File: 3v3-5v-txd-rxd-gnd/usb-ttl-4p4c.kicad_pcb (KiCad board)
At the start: 4 copper layers, 41.3 x 14 mm, 3 parts, among them J1 4P4C, P1 CONN_5X1

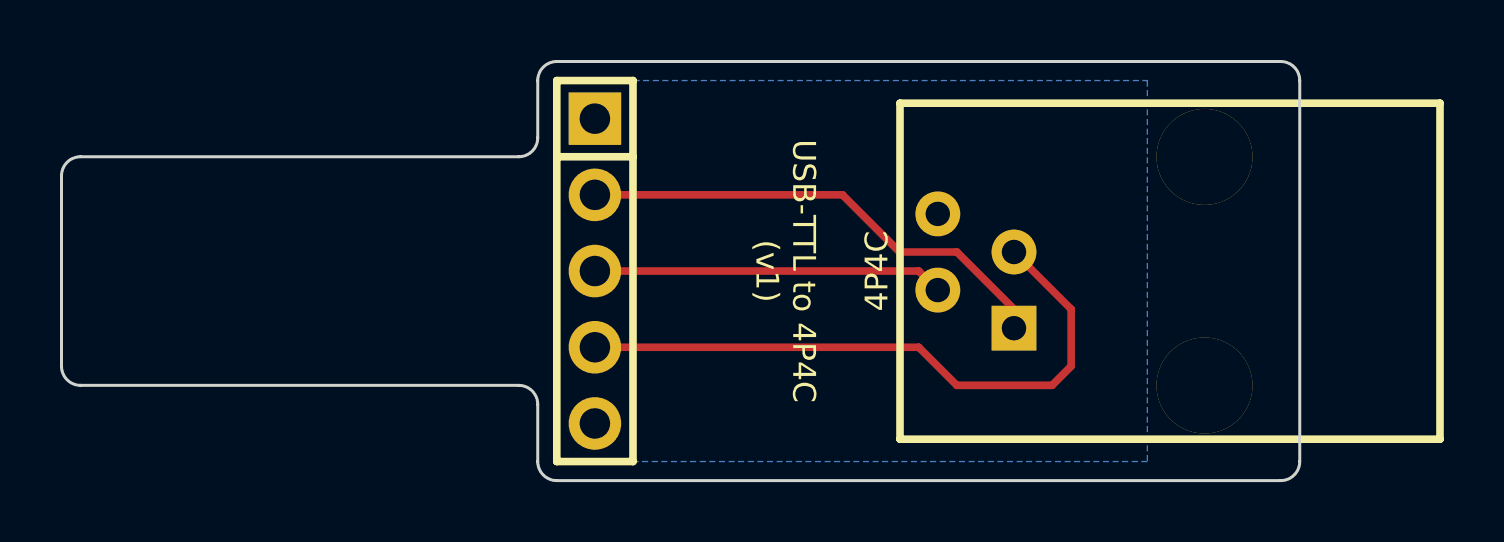
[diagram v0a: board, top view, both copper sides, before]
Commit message: adding a diode
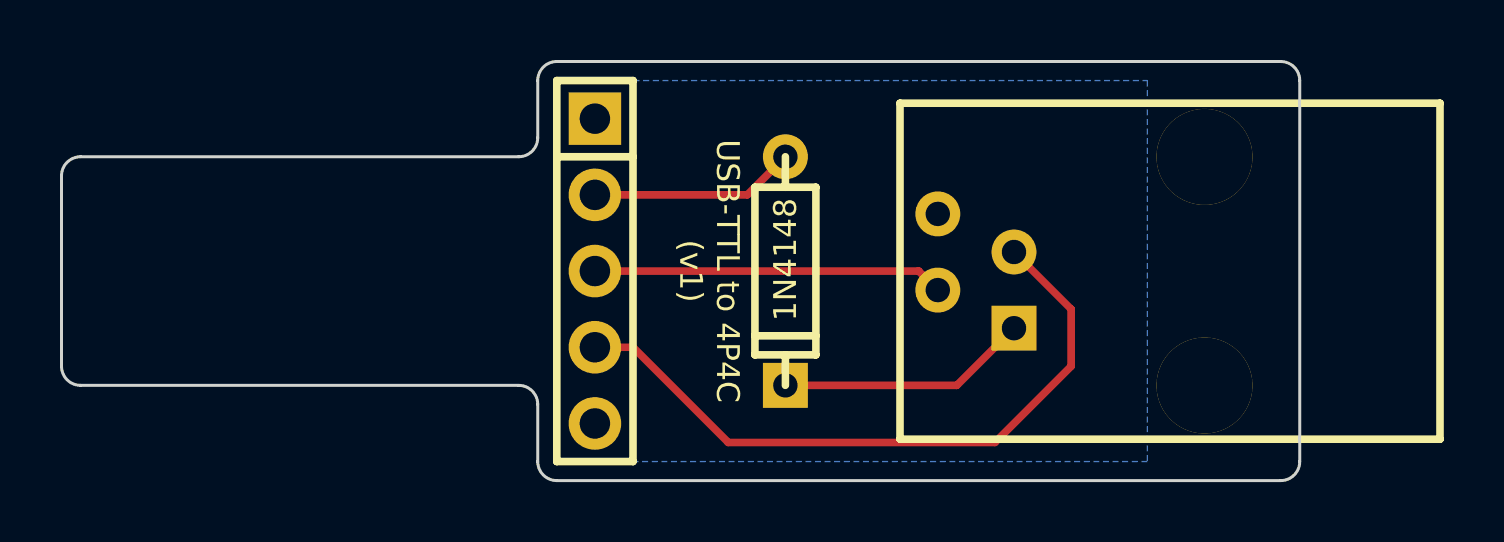
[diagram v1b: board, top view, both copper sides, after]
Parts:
- added D1: 1N4148, DIODE_SS_059A_03_PL, F.Cu at (180.3, 111.1)
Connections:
- J1 pad 1: 5V -> N-000006
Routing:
- net 5V: track 16.2 -> 6.88 mm
- net N-000006: track 0.00 -> 8.41 mm
- net RXD: track 21.3 -> 22.8 mm
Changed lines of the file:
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@@
 (kicad_pcb (version 3) (host pcbnew "(22-Jun-2014 BZR 4027)-stable")
   (general
-    (links 4)
+    (links 5)
     (no_connects 0)
-    (area 156.159999 104.089999 202.541001 118.160001)
+    (area 156.159999 104.089999 197.535001 118.160001)
     (thickness 1.6)
     (drawings 27)
-    (tracks 13)
+    (tracks 12)
     (zones 0)
-    (modules 3)
-    (nets 5)
+    (modules 4)
+    (nets 6)
   )
   (page A3)
@@
     (2 Inner2.Cu signal)
     (1 Inner1.Cu signal)
-    (0 B.Cu signal hide)
+    (0 B.Cu signal)
     (16 B.Adhes user)
     (17 F.Adhes user)
@@
   (net 1 5V)
   (net 2 GND)
-  (net 3 RXD)
-  (net 4 TXD)
+  (net 3 N-000006)
+  (net 4 RXD)
+  (net 5 TXD)
   (net_class Default "This is the default net class."
     (clearance 0.254)
@@
     (add_net 5V)
     (add_net GND)
+    (add_net N-000006)
     (add_net RXD)
     (add_net TXD)
@@
     (pad 3 thru_hole circle (at 2.54 0 270) (size 1.7526 1.7526) (drill 1.016)
       (layers *.Cu *.Mask F.SilkS)
-      (net 4 TXD)
+      (net 5 TXD)
     )
     (pad 4 thru_hole circle (at 5.08 0 270) (size 1.7526 1.7526) (drill 1.016)
       (layers *.Cu *.Mask F.SilkS)
-      (net 3 RXD)
+      (net 4 RXD)
     )
     (pad 5 thru_hole circle (at 7.62 0 270) (size 1.7526 1.7526) (drill 1.016)
@@
       (effects (font (size 1.016 1.016) (thickness 0.2032)))
     )
-    (fp_text value 4P4C (at 1.905 -4.572 90) (layer F.SilkS)
+    (fp_text value 4P4C (at 1.905 -4.572 90) (layer F.SilkS) hide
       (effects (font (size 0.762 0.762) (thickness 0.1524)))
     )
@@
     (pad 2 thru_hole circle (at 1.27 -2.54 90) (size 1.4986 1.4986) (drill 0.8128)
       (layers *.Cu *.Mask F.SilkS)
-      (net 4 TXD)
+      (net 5 TXD)
     )
     (pad 4 thru_hole circle (at 3.81 -2.54 90) (size 1.4986 1.4986) (drill 0.8128)
@@
     (pad 1 thru_hole rect (at 0 0 90) (size 1.4986 1.4986) (drill 0.8128)
       (layers *.Cu *.Mask F.SilkS)
-      (net 1 5V)
+      (net 3 N-000006)
     )
     (pad 3 thru_hole circle (at 2.54 0 90) (size 1.4986 1.4986) (drill 0.8128)
       (layers *.Cu *.Mask F.SilkS)
-      (net 3 RXD)
+      (net 4 RXD)
     )
     (pad "" thru_hole circle (at 5.71 6.35 90) (size 3.2 3.2) (drill 3.2)
@@
       (xy 0.90932 1.3462)) (layer B.SilkS) (width 0.00254))
   )
-  (gr_text "USB-TTL to 4P4C\n(v1)" (at 180.34 111.125 270) (layer F.SilkS)
+  (module DIODE_SS_059A_03_PL (layer F.Cu)
+    (at 180.34 111.125 270)
+    (descr "Small-signal diode, 0.3\"")
+    (tags "DIODE DEV")
+    (fp_text reference D1 (at 0 -1.651 270) (layer F.SilkS) hide
+      (effects (font (size 0.762 0.762) (thickness 0.1524)))
+    )
+    (fp_text value 1N4148 (at -0.381 0 270) (layer F.SilkS)
+      (effects (font (size 0.762 0.762) (thickness 0.1524)))
+    )
+    (fp_line (start -2.794 0) (end -3.81 0) (layer F.SilkS) (width 0.254))
+    (fp_line (start 2.794 0) (end 3.81 0) (layer F.SilkS) (width 0.254))
+    (fp_line (start -2.794 1.016) (end 2.794 1.016) (layer F.SilkS) (width 0.254))
+    (fp_line (start 2.794 -1.016) (end -2.794 -1.016) (layer F.SilkS) (width 0.254))
+    (fp_line (start 2.159 -1.016) (end 2.159 1.016) (layer F.SilkS) (width 0.254))
+    (fp_line (start 2.794 0) (end 2.794 -1.016) (layer F.SilkS) (width 0.254))
+    (fp_line (start -2.794 -1.016) (end -2.794 0) (layer F.SilkS) (width 0.254))
+    (fp_line (start -2.794 0) (end -2.794 1.016) (layer F.SilkS) (width 0.254))
+    (fp_line (start 2.794 1.016) (end 2.794 0) (layer F.SilkS) (width 0.254))
+    (pad 2 thru_hole rect (at 3.81 0 270) (size 1.4986 1.4986) (drill 0.8128)
+      (layers *.Cu *.Mask F.SilkS)
+      (net 3 N-000006)
+    )
+    (pad 1 thru_hole oval (at -3.81 0 270) (size 1.4986 1.4986) (drill 0.8128)
+      (layers *.Cu *.Mask F.SilkS)
+      (net 1 5V)
+    )
+    (model discret/diode.wrl
+      (at (xyz 0 0 0))
+      (scale (xyz 0.3 0.3 0.3))
+      (rotate (xyz 0 0 0))
+    )
+  )
+  (gr_text "USB-TTL to 4P4C\n(v1)" (at 177.8 111.125 270) (layer F.SilkS)
     (effects (font (size 0.762 0.762) (thickness 0.1524)))
   )
@@
     (effects (font (size 0.762 0.762) (thickness 0.1524)) (justify right mirror))
   )
-  (segment (start 173.99 108.585) (end 182.245 108.585) (width 0.254) (layer F.Cu) (net 1))
-  (segment (start 187.96 112.395) (end 187.96 113.03) (width 0.254) (layer F.Cu) (net 1))
-  (segment (start 186.055 110.49) (end 187.96 112.395) (width 0.254) (layer F.Cu) (net 1))
-  (segment (start 184.15 110.49) (end 186.055 110.49) (width 0.254) (layer F.Cu) (net 1))
-  (segment (start 182.245 108.585) (end 184.15 110.49) (width 0.254) (layer F.Cu) (net 1))
-  (segment (start 173.99 113.665) (end 184.785 113.665) (width 0.254) (layer F.Cu) (net 3))
-  (segment (start 189.865 112.395) (end 187.96 110.49) (width 0.254) (layer F.Cu) (net 3))
-  (segment (start 189.865 114.3) (end 189.865 112.395) (width 0.254) (layer F.Cu) (net 3))
-  (segment (start 189.23 114.935) (end 189.865 114.3) (width 0.254) (layer F.Cu) (net 3))
-  (segment (start 186.055 114.935) (end 189.23 114.935) (width 0.254) (layer F.Cu) (net 3))
-  (segment (start 184.785 113.665) (end 186.055 114.935) (width 0.254) (layer F.Cu) (net 3))
-  (segment (start 173.99 111.125) (end 184.785 111.125) (width 0.254) (layer F.Cu) (net 4))
-  (segment (start 184.785 111.125) (end 185.42 111.76) (width 0.254) (layer F.Cu) (net 4))
+  (segment (start 173.99 108.585) (end 179.07 108.585) (width 0.254) (layer F.Cu) (net 1) (status 400000))
+  (segment (start 179.07 108.585) (end 180.34 107.315) (width 0.254) (layer F.Cu) (net 1) (status 800000))
+  (segment (start 180.34 114.935) (end 186.055 114.935) (width 0.254) (layer F.Cu) (net 3) (status 400000))
+  (segment (start 186.055 114.935) (end 187.96 113.03) (width 0.254) (layer F.Cu) (net 3) (status 800000))
+  (segment (start 173.99 113.665) (end 175.26 113.665) (width 0.254) (layer F.Cu) (net 4) (status 400000))
+  (segment (start 189.865 112.395) (end 187.96 110.49) (width 0.254) (layer F.Cu) (net 4) (status 800000))
+  (segment (start 189.865 114.3) (end 189.865 112.395) (width 0.254) (layer F.Cu) (net 4))
+  (segment (start 187.325 116.84) (end 189.865 114.3) (width 0.254) (layer F.Cu) (net 4))
+  (segment (start 178.435 116.84) (end 187.325 116.84) (width 0.254) (layer F.Cu) (net 4))
+  (segment (start 175.26 113.665) (end 178.435 116.84) (width 0.254) (layer F.Cu) (net 4))
+  (segment (start 173.99 111.125) (end 184.785 111.125) (width 0.254) (layer F.Cu) (net 5))
+  (segment (start 184.785 111.125) (end 185.42 111.76) (width 0.254) (layer F.Cu) (net 5))
   (zone (net 2) (net_name GND) (layer B.Cu) (hatch edge 0.508)
     (connect_pads (clearance 0.508))
